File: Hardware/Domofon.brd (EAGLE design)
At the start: 88.9 x 52.1 mm, 82 parts, among them J3 USB_A_PTH_MALE, Q1 BC817-40SMD, Q2 BC817-40SMD, Q3 BC817-40SMD, Q4 BC817-40SMD, Q5 SS8050-G, Q6 SS8050-G, U1 IP5306, U2 ESP-WROOM-32EU, U3 AMS1117, U4 CH340K, U5 PAM8403

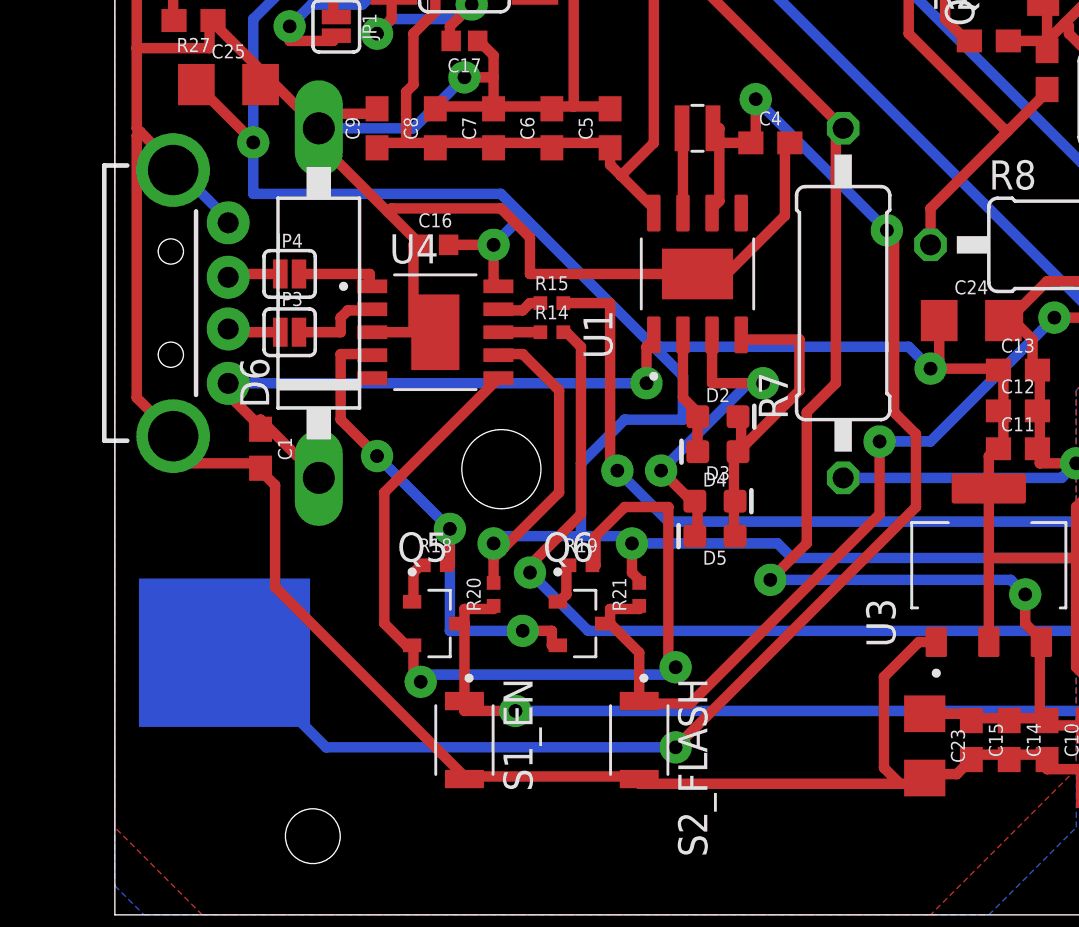
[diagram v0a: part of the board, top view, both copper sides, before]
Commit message: Защита от скачков по USB
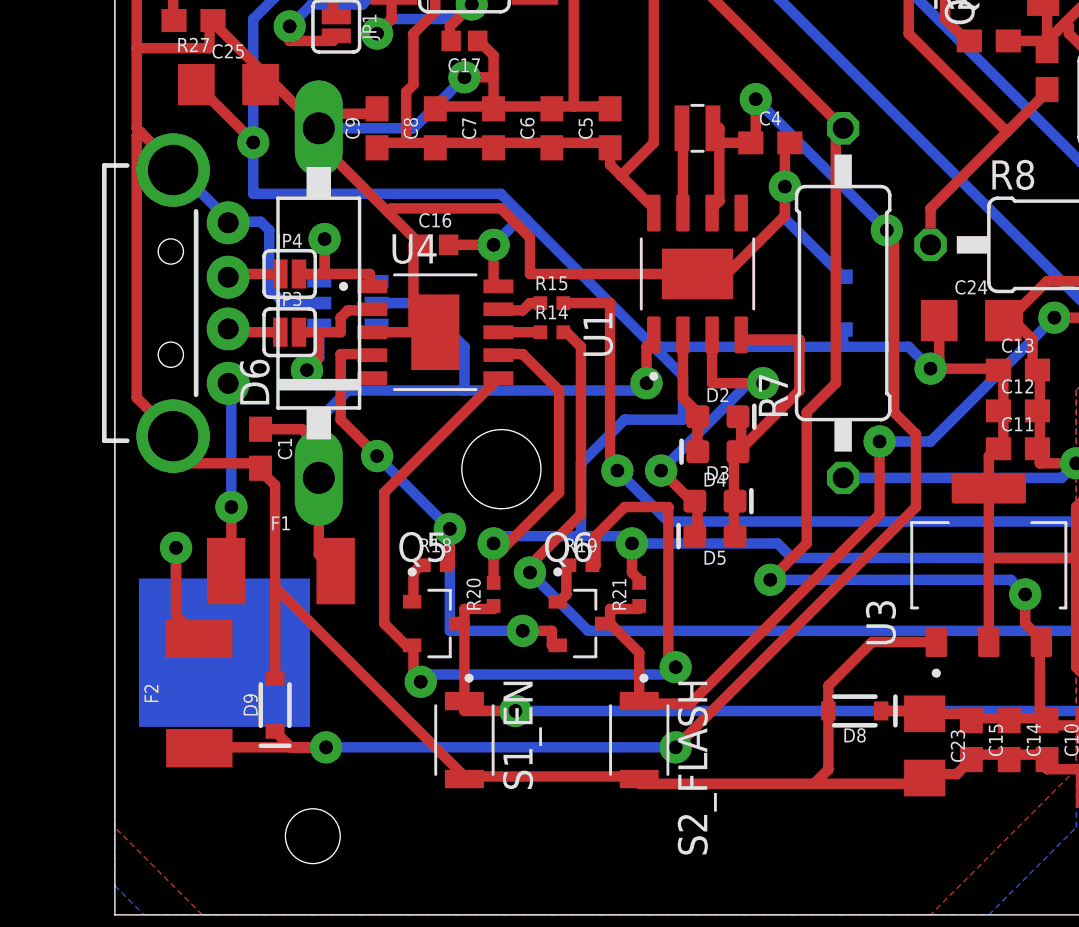
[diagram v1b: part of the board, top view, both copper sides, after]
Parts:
- added D7, D8, D9: 5.6V, SparkFun-DiscreteSemi:SOD-323
- added F1, F2: 16V/2.5A(5A TRIP), SparkFun-Fuses:1812
- added U6: AZC099-04S, SamacSys_Parts:SOT95P275X110-6N
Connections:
- new net N$43: F1.1, J3.VBUS
- new net N$44: BT2.P, F2.2
- net 3.3V: now also D7.C
- net 5V: now also D8.C
- net GND: now also D7.A, D8.A, D9.A, U6.2
- net N$19: now also D9.C, F2.1; no longer BT2.P
- net N$5: now also F1.2, U6.5; no longer J3.VBUS
- net USBU_DM: now also U6.1
- net USBU_DP: now also U6.3
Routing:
- net GND: track 452.9 -> 471.4 mm, vias 4 -> 5
- net N$44: track 0.00 -> 10.4 mm, vias 0 -> 1
- net N$43: track 0.00 -> 8.34 mm, vias 0 -> 1
- net N$5: track 27.0 -> 34.9 mm
- net USBU_DM: track 3.97 -> 8.03 mm, vias 0 -> 1
- net USBU_DP: track 3.65 -> 7.12 mm, vias 0 -> 1
- net 5V: track 117.8 -> 119.7 mm
- net N$19: track 65.2 -> 67.1 mm, vias 3 -> 4
- net 3.3V: track 211.0 -> 211.7 mm
